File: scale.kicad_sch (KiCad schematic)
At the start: 0 parts

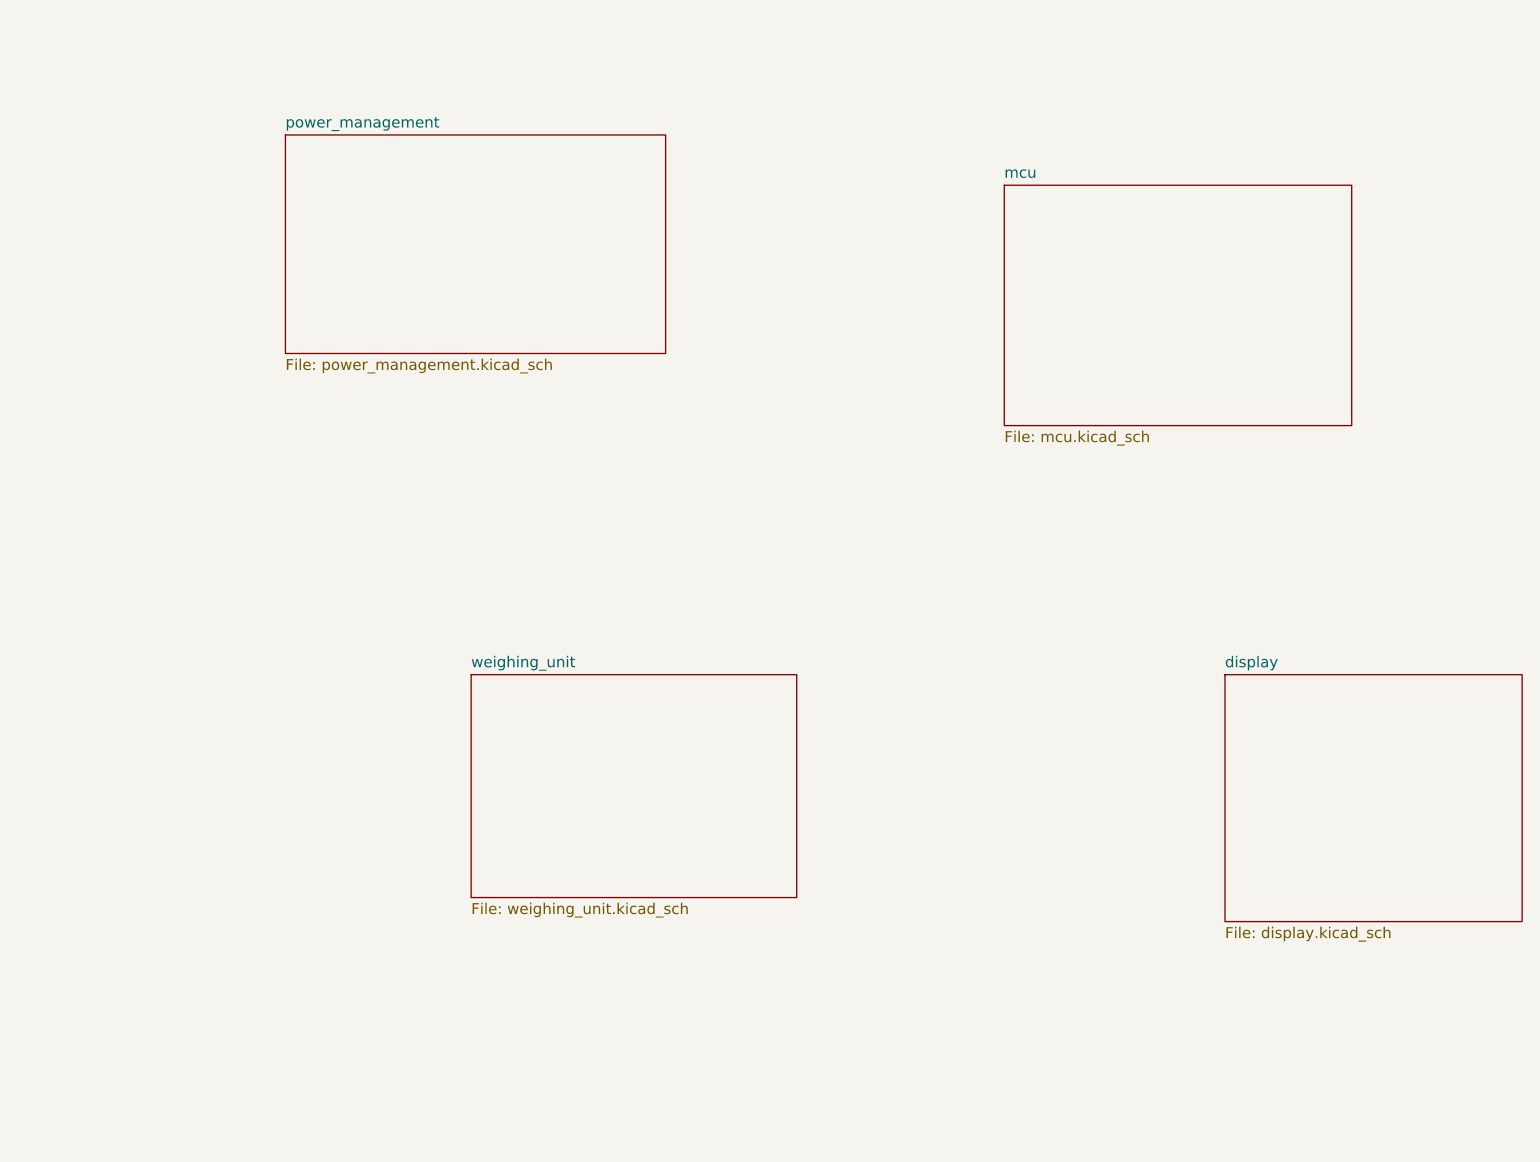
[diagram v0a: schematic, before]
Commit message: add mcu, sensor, sensor inst, power
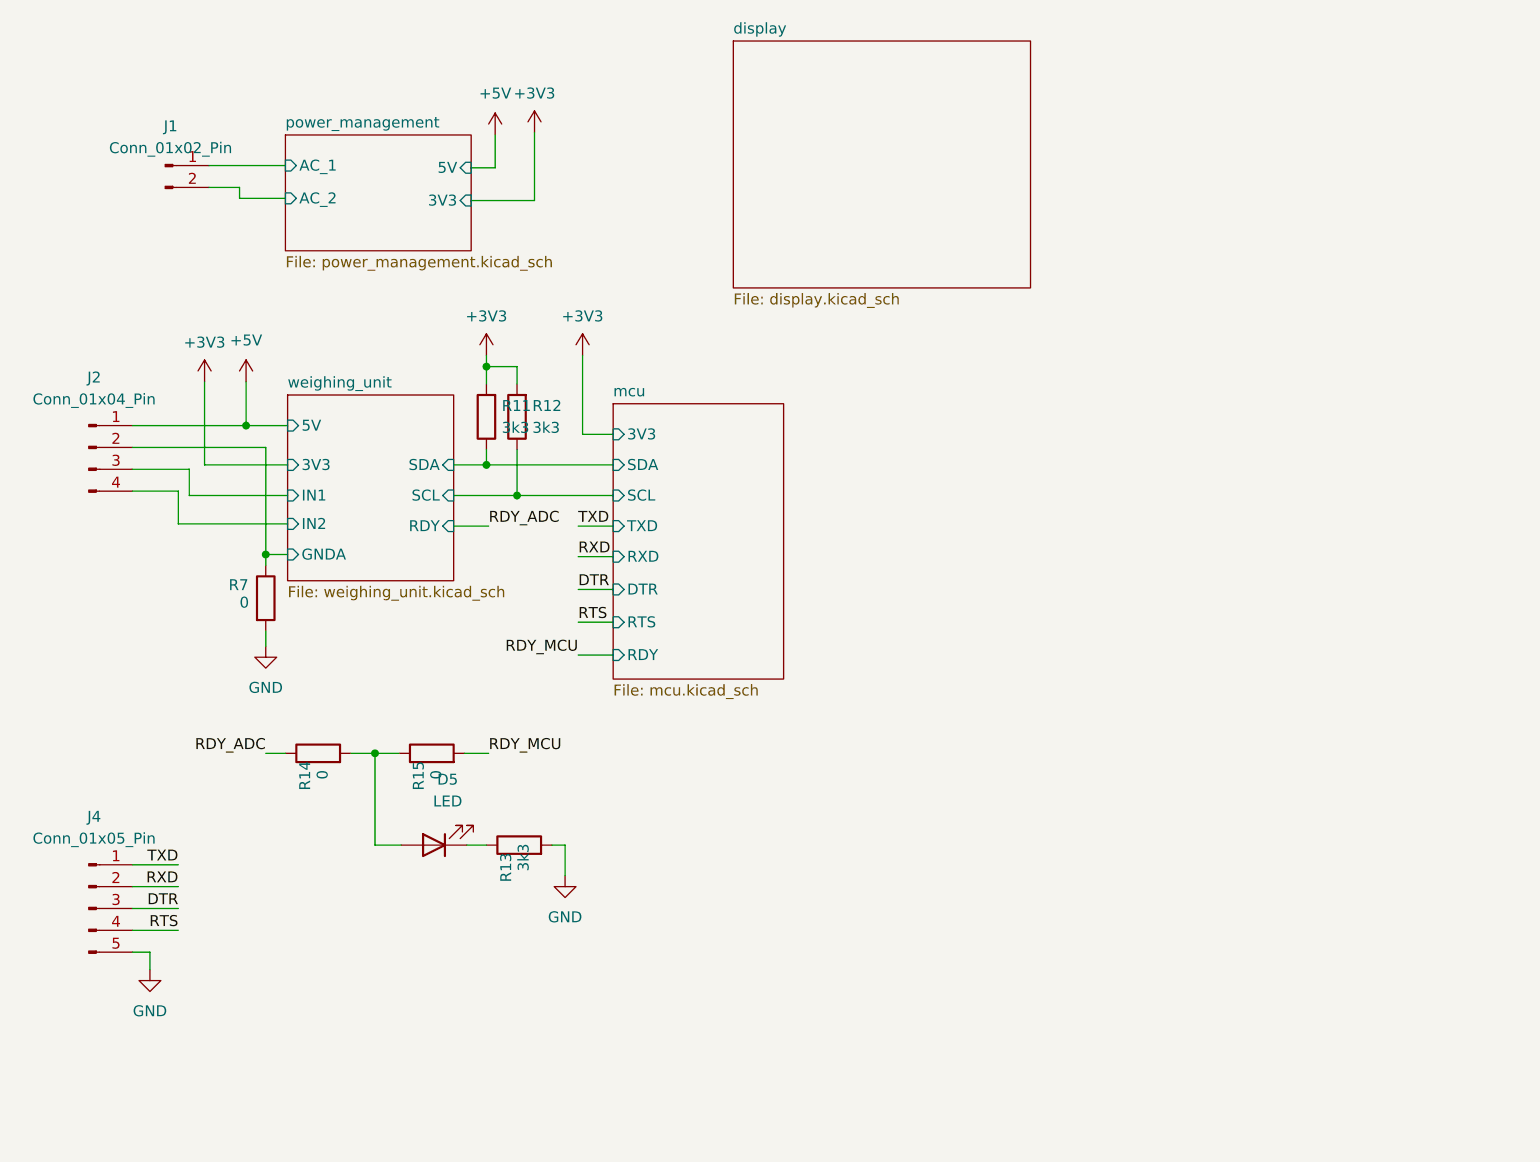
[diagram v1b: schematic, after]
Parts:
- added D5: LED, LED_SMD:LED_0805_2012Metric, symbol Device:LED
- added J1: Conn_01x02_Pin, symbol Connector:Conn_01x02_Pin
- added J2: Conn_01x04_Pin, symbol Connector:Conn_01x04_Pin
- added J4: Conn_01x05_Pin, symbol Connector:Conn_01x05_Pin
- added R11, R12, R13: 3k3, Resistor_SMD:R_0805_2012Metric, symbol Device:R
- added R14, R15: 0, Resistor_SMD:R_0402_1005Metric, symbol Device:R
- added R7: 0, Resistor_SMD:R_0805_2012Metric, symbol Device:R
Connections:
- new net: D5.2 (A), R14.2, R15.1
- new net: D5.1 (K), R13.1
- new net +3V3: R11.2, R12.2
- new net +5V: J2.1 (Pin_1)
- new net DTR: J4.3 (Pin_3)
- new net GND: J4.5 (Pin_5), R13.2, R7.2
- new net RDY_ADC: R14.1
- new net RDY_MCU: R15.2
- new net RTS: J4.4 (Pin_4)
- new net RXD: J4.2 (Pin_2)
- new net TXD: J4.1 (Pin_1)
- new net mcu/SCL: R12.1
- new net mcu/SDA: R11.1
- new net power_management/AC_1: J1.1 (Pin_1)
- new net power_management/AC_2: J1.2 (Pin_2)
- new net weighing_unit/GNDA: J2.2 (Pin_2), R7.1
- new net weighing_unit/IN1: J2.3 (Pin_3)
- new net weighing_unit/IN2: J2.4 (Pin_4)
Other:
- sheet mcu ports: added 3V3, DTR, RDY, RTS, RXD, SCL, SDA, TXD; removed none
- sheet power_management ports: added 3V3, 5V, AC_1, AC_2; removed none
- sheet weighing_unit ports: added 3V3, 5V, GNDA, IN1, IN2, RDY, SCL, SDA; removed none

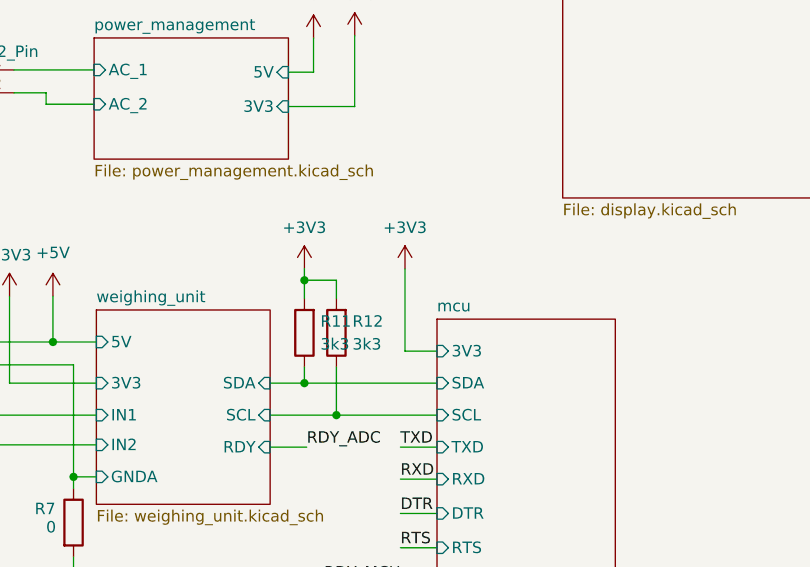
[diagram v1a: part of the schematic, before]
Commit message: add initial display circuit
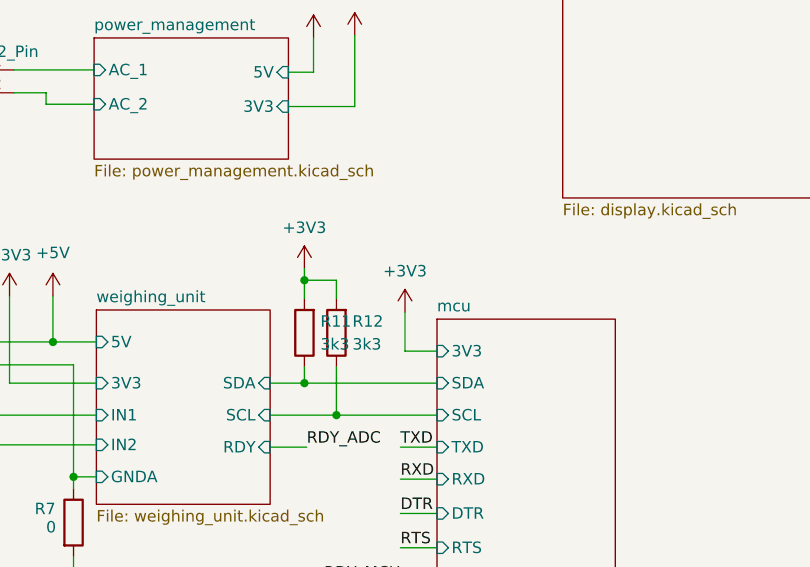
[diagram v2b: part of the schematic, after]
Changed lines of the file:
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@@
+    (stroke (width 0) (type default))
+  )
+  (wire (pts (xy 80.518 74.676) (xy 80.518 78.994))
     (stroke (width 0) (type default))
   )
@@
   )
   (wire (pts (xy 80.01 104.648) (xy 84.074 104.648))
-    (stroke (width 0) (type default))
-  )
-  (wire (pts (xy 80.518 78.994) (xy 80.518 69.85))
     (stroke (width 0) (type default))
   )
@@
     )
   )
-  (symbol (lib_id "power:+3V3") (at 80.518 69.85 0) (unit 1)
-    (in_bom yes) (on_board yes) (dnp no) (fields_autoplaced)
-    (property "Reference" "#PWR026" (at 80.518 73.66 0)
-      (effects (font (size 1.27 1.27)) hide)
-    )
-    (property "Value" "+3V3" (at 80.518 65.278 0)
-      (effects (font (size 1.27 1.27)))
-    )
-    (property "Footprint" "" (at 80.518 69.85 0)
-      (effects (font (size 1.27 1.27)) hide)
-    )
-    (property "Datasheet" "" (at 80.518 69.85 0)
-      (effects (font (size 1.27 1.27)) hide)
-    )
+  (symbol (lib_id "power:+3V3") (at 80.518 74.676 0) (unit 1)
+    (in_bom yes) (on_board yes) (dnp no) (fields_autoplaced)
+    (property "Reference" "#PWR026" (at 80.518 78.486 0)
+      (effects (font (size 1.27 1.27)) hide)
+    )
+    (property "Value" "+3V3" (at 80.518 70.104 0)
+      (effects (font (size 1.27 1.27)))
+    )
+    (property "Footprint" "" (at 80.518 74.676 0)
+      (effects (font (size 1.27 1.27)) hide)
+    )
+    (property "Datasheet" "" (at 80.518 74.676 0)
+      (effects (font (size 1.27 1.27)) hide)
+    )
